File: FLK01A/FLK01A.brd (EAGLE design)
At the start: 30.5 x 30.5 mm, 30 parts, among them J1 M10SMD_MALE_SHORT, J2 M10SMD_MALE_SHORT, U1 LPC812TSSOP20, U2 EKMBTO5, U3 HTU21DSMD, U4 MMA8452Q, U5 VCNL4000, U6 MPL3115A2LGA8, Y1 12MHZ

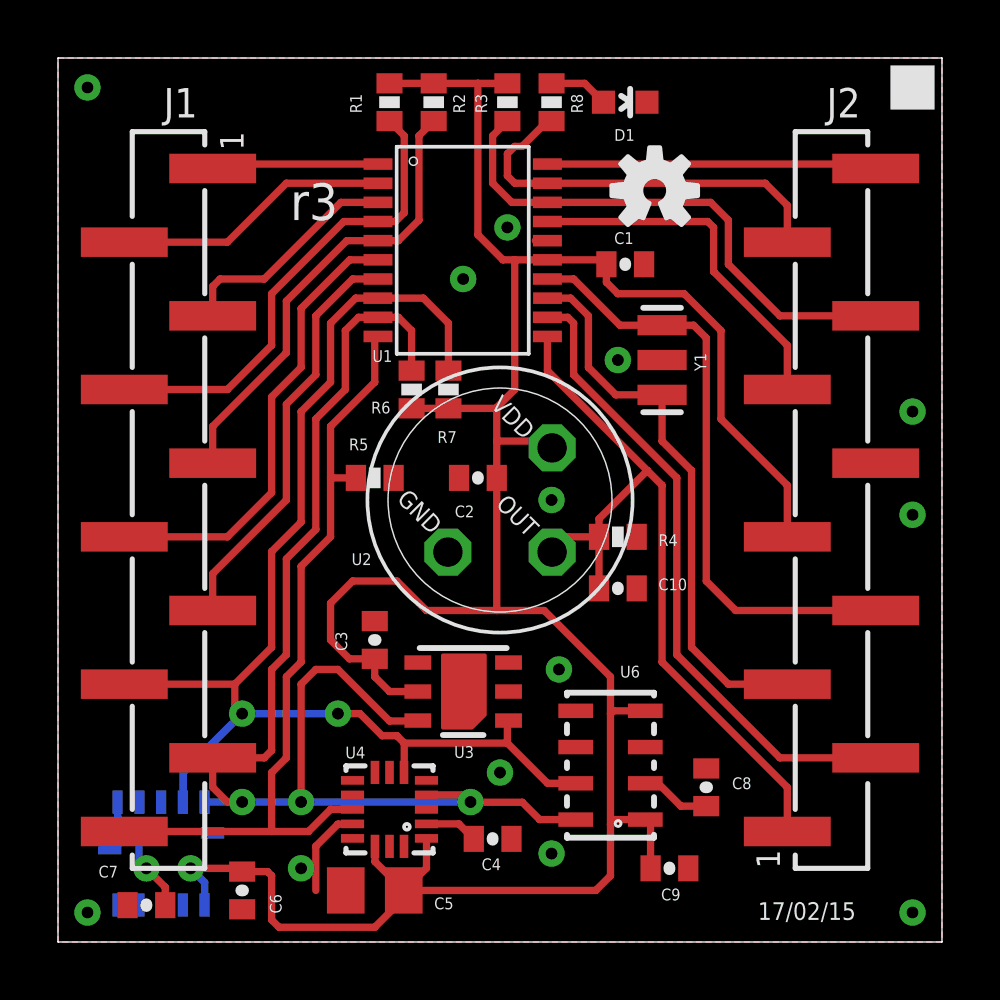
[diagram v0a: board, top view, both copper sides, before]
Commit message: [flk/flr] adapt board layout to new M10 footprints + power switch
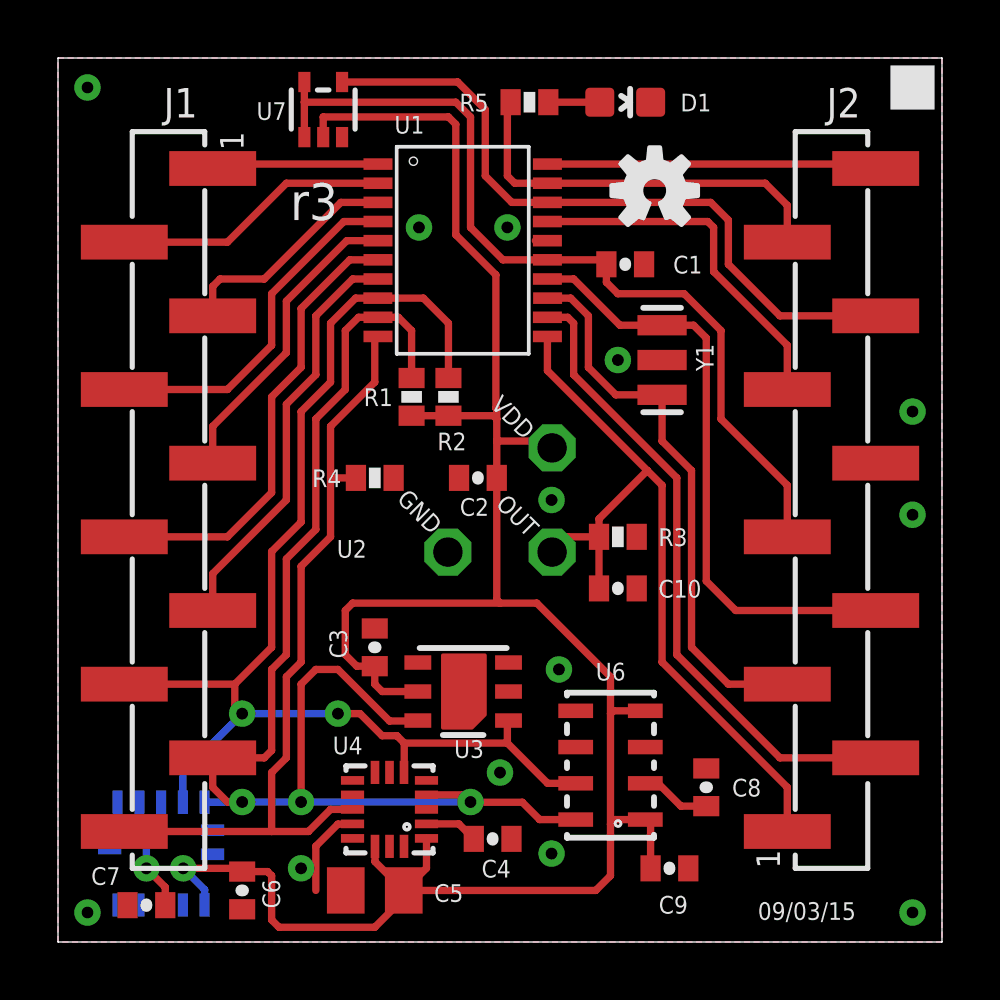
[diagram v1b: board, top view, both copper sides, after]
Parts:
- removed R6, R7: 4k7, SparkFun-Passives:0402-RES
- removed R8: 1k, SparkFun-Passives:0402-RES
- added U7: (no value), flukso:SOT353
- R1, R2: value 100k -> 4k7
- R3: value 2M -> 100k
- R5: value 100k -> 1k
- U5: value VCNL4000 -> VCNL4010; device SparkFun-Sensors:VCNL4000 -> flukso:VCNL4010
- moved R3 15.5 mm to (19.3, 14.0), turned to 180 degrees
- moved R5 14.0 mm to (16.3, 29.0)
- moved R1 10.2 mm to (12.2, 18.8), turned to 270 degrees
- moved R2 10.2 mm to (13.5, 18.8), turned to 270 degrees
- moved R4 8.62 mm to (10.9, 16.0)
- moved C3 0.25 mm to (10.9, 10.2)
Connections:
- new net VDD: C1.1, J2.5, U1.15, U7.1, U7.5
- net !RESET!: no longer R1.1
- net 3.3V: now also U7.2; no longer C1.1, J2.5, R3.2, R6.2, R7.2, U1.15
- net EKMB_INT: now also R3.2; no longer R4.2
- net GND: now also R3.1, U5.13, U7.3; no longer R5.1, U5.6
- net I2C0_SCL: now also R1.1; no longer R6.1
- net I2C0_SDA: now also R2.1; no longer R7.1
- net ISP_RXD: now also R5.2; no longer R8.2
- net ISP_TXD: no longer R2.1
- net MMA_INT: now also R4.2; no longer R5.2
- net N$8: now also R5.1; no longer R8.1
- net PIO0_6: now also U7.4; no longer R3.1
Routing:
- net VDD: track 0.00 -> 30.2 mm
- net 3.3V: track 95.5 -> 77.1 mm
- net PIO0_6: track 18.3 -> 24.2 mm
- net ISP_TXD: track 16.0 -> 10.7 mm
- net !RESET!: track 16.6 -> 12.2 mm
- net GND: vias 14 -> 13
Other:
- board text added: "09/03/15"
- board text removed: "17/02/15"

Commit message: [flk] connect VCNL4010 int pin to LPC812
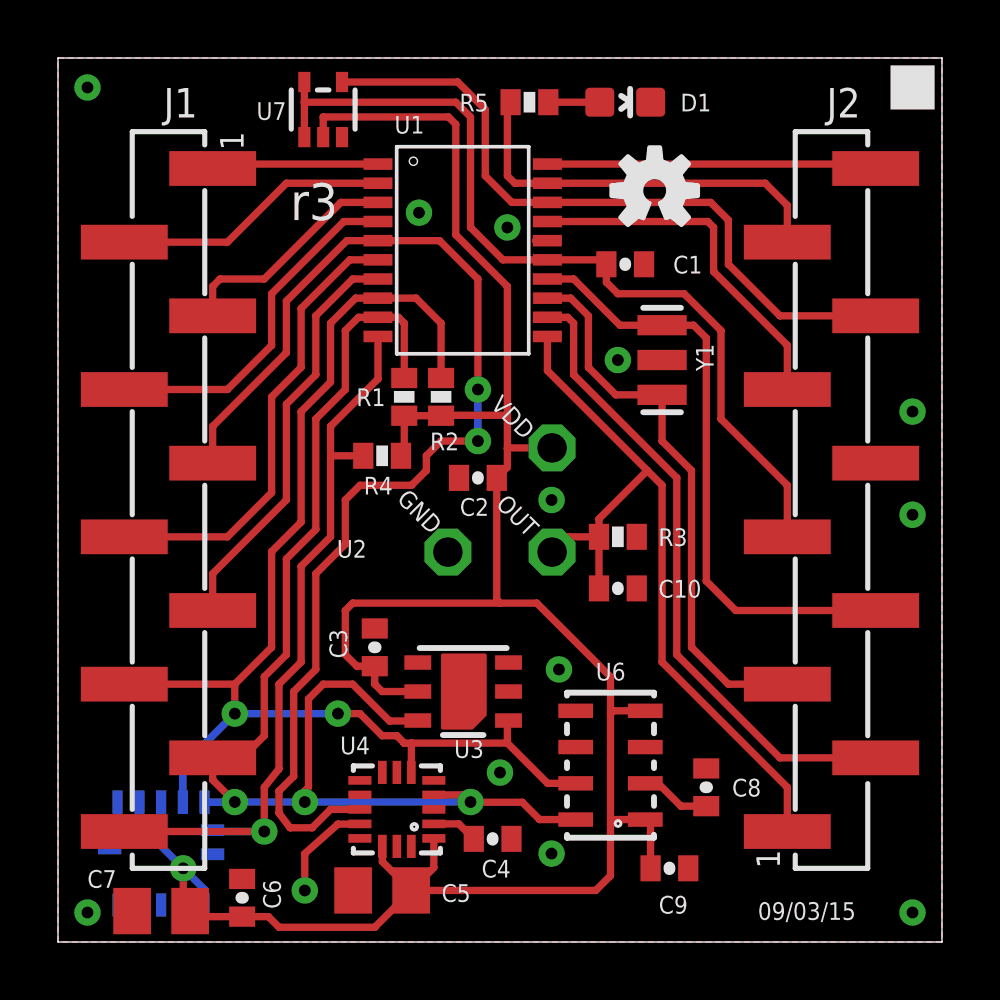
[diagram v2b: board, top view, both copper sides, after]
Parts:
- C7: value 100nF -> 4.7uF; device flukso:0402-CAP -> flukso:C0805K
- moved R4 0.80 mm to (11.2, 16.8), turned to 0 degrees
- moved C7 0.55 mm to (3.56, 1.07)
- moved C6 0.25 mm to (6.35, 1.52), turned to 90 degrees
- moved C5 0.25 mm to (11.2, 1.78)
- moved R1 0.25 mm to (11.9, 18.8)
- moved R2 0.25 mm to (13.2, 18.8)
- moved U4 0.25 mm to (11.7, 4.57)
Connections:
- removed net MMA_INT: J1.10, R4.2, U1.10, U4.11
- removed net N$1: C7.1, U5.1
- new net VCNL_INT: J1.10, R4.1, U1.10, U5.6
- net 3.3V: now also C7.1, R4.2, U5.1
- net GND: no longer R4.1
- net ISP_TXD: now also U4.11
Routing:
- net ISP_TXD: track 10.7 -> 41.0 mm, vias 0 -> 2
- net MMA_INT: track 27.6 -> 0.00 mm
- net VCNL_INT: track 0.00 -> 26.4 mm, vias 0 -> 1
- net 3.3V: track 77.1 -> 82.2 mm
- net N$1: track 4.23 -> 0.00 mm, vias 1 -> 0
- net I2C0_SCL: track 47.9 -> 46.1 mm
